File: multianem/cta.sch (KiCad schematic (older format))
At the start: 146 parts, among them Q1 TIP120, Q2 TIP120, Q3 TIP120, Q4 TIP120, Q5 TIP120, Q6 TIP120, Q7 TIP120, Q8 TIP120, U1 OP07, U2 OP07, U3 OP07, U4 OP07, U5 OP07, U6 OP07, U7 OP07, U8 OP07

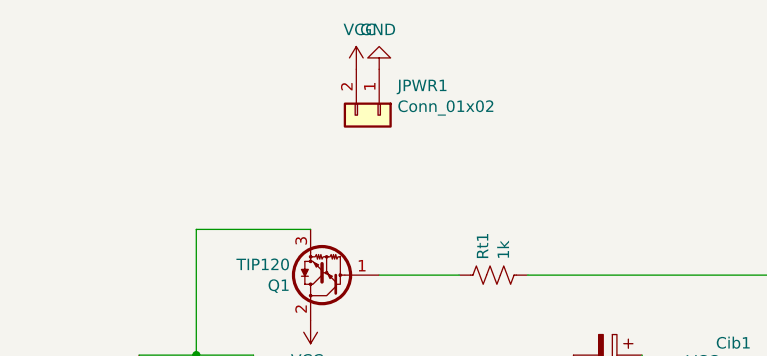
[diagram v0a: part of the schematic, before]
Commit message: Added more power inputs to the board
To make it easy to stack the 8 channel boards, added a Vcc and GND inputs.
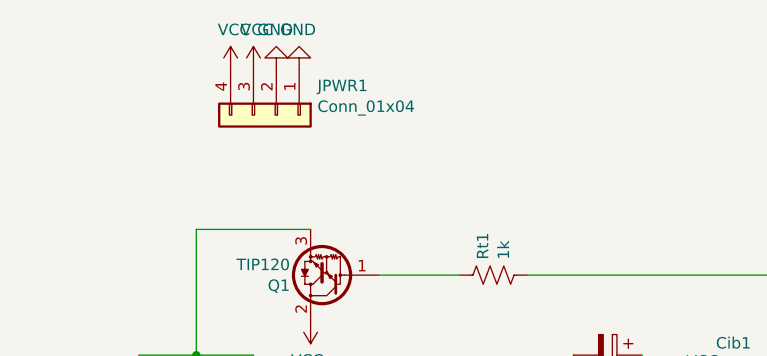
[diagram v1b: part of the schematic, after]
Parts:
- removed JPWR1: Conn_01x02, TerminalBlock:TerminalBlock_bornier-2_P5.08mm, symbol Connector_Generic:Conn_01x02
- added JPWR1: Conn_01x04, TerminalBlock:TerminalBlock_bornier-4_P5.08mm, symbol Connector_Generic:Conn_01x04
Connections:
- net GND: now also JPWR1.1 (Pin_1), JPWR1.2 (Pin_2)
- net VCC: now also JPWR1.3 (Pin_3), JPWR1.4 (Pin_4)
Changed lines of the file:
@@
 $EndComp
 $Comp
-L Connector_Generic:Conn_01x02 JPWR1
-U 1 1 605109A3
-P 1800 1100
-F 0 "JPWR1" V 1672 1180 50  0000 L CNN
-F 1 "Conn_01x02" V 1763 1180 50  0000 L CNN
-F 2 "TerminalBlock:TerminalBlock_bornier-2_P5.08mm" H 1800 1100 50  0001 C CNN
-F 3 "~" H 1800 1100 50  0001 C CNN
-	1    1800 1100
-	0    1    1    0
-$EndComp
-$Comp
-L power:GND #PWR06
-U 1 1 60511F0B
-P 1800 900
-F 0 "#PWR06" H 1800 650 50  0001 C CNN
-F 1 "GND" H 1805 727 50  0000 C CNN
-F 2 "" H 1800 900 50  0001 C CNN
-F 3 "" H 1800 900 50  0001 C CNN
-	1    1800 900
-	-1   0    0    1
-$EndComp
-$Comp
-L power:VCC #PWR05
-U 1 1 60513FB5
-P 1700 900
-F 0 "#PWR05" H 1700 750 50  0001 C CNN
-F 1 "VCC" H 1715 1073 50  0000 C CNN
-F 2 "" H 1700 900 50  0001 C CNN
-F 3 "" H 1700 900 50  0001 C CNN
-	1    1700 900
-	1    0    0    -1
-$EndComp
-$Comp
 L Amplifier_Operational:OP07 U1
 U 1 1 60488266
@@
 Text Label 14050 7200 3    50   ~ 0
 V1
+$Comp
+L Connector_Generic:Conn_01x04 JPWR1
+U 1 1 60802D44
+P 1350 1100
+F 0 "JPWR1" V 1222 1280 50  0000 L CNN
+F 1 "Conn_01x04" V 1313 1280 50  0000 L CNN
+F 2 "TerminalBlock:TerminalBlock_bornier-4_P5.08mm" H 1350 1100 50  0001 C CNN
+F 3 "~" H 1350 1100 50  0001 C CNN
+	1    1350 1100
+	0    1    1    0
+$EndComp
+$Comp
+L power:GND #PWR0194
+U 1 1 608037F7
+P 1450 900
+F 0 "#PWR0194" H 1450 650 50  0001 C CNN
+F 1 "GND" H 1455 727 50  0000 C CNN
+F 2 "" H 1450 900 50  0001 C CNN
+F 3 "" H 1450 900 50  0001 C CNN
+	1    1450 900
+	-1   0    0    1
+$EndComp
+$Comp
+L power:GND #PWR0195
+U 1 1 608041DA
+P 1350 900
+F 0 "#PWR0195" H 1350 650 50  0001 C CNN
+F 1 "GND" H 1355 727 50  0000 C CNN
+F 2 "" H 1350 900 50  0001 C CNN
+F 3 "" H 1350 900 50  0001 C CNN
+	1    1350 900
+	-1   0    0    1
+$EndComp
+$Comp
+L power:VCC #PWR0196
+U 1 1 60804C71
+P 1250 900
+F 0 "#PWR0196" H 1250 750 50  0001 C CNN
+F 1 "VCC" H 1265 1073 50  0000 C CNN
+F 2 "" H 1250 900 50  0001 C CNN
+F 3 "" H 1250 900 50  0001 C CNN
+	1    1250 900
+	1    0    0    -1
+$EndComp
+$Comp
+L power:VCC #PWR0197
+U 1 1 608057C6
+P 1150 900
+F 0 "#PWR0197" H 1150 750 50  0001 C CNN
+F 1 "VCC" H 1165 1073 50  0000 C CNN
+F 2 "" H 1150 900 50  0001 C CNN
+F 3 "" H 1150 900 50  0001 C CNN
+	1    1150 900
+	1    0    0    -1
+$EndComp
 $EndSCHEMATC
